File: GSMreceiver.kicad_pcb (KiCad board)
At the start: 2 copper layers, 69 x 83 mm, 136 parts, among them J1 Conn_01x06_Pin, J10 Conn_01x05, J11 Conn_DEGSON_01x02_Pin, J2 Conn_02x02_2.54, J3 Conn_DEGSON_01x02_Pin, J4 Conn_DEGSON_01x02_Pin, J5 Conn_DEGSON_01x02_Pin, J6 Conn_DEGSON_01x02_Pin, J7 Conn_DEGSON_01x02_Pin, J8 1042240820, J9 HJ-SMA405, Q1 BC848, Q2 BC848, SW1 SM5-180UP-1, U1 STM32L052C8Tx, U10 TLV76033, U2 PRAG71S, U3 PRAG71S, U4 PRAG71S, U5 PRAG71S, U6 TPS62177DQC, U7 TPS5430DDA, U8 SIM800C, U9 ST485E, Y1 4 MHz, Y2 32768 kHz

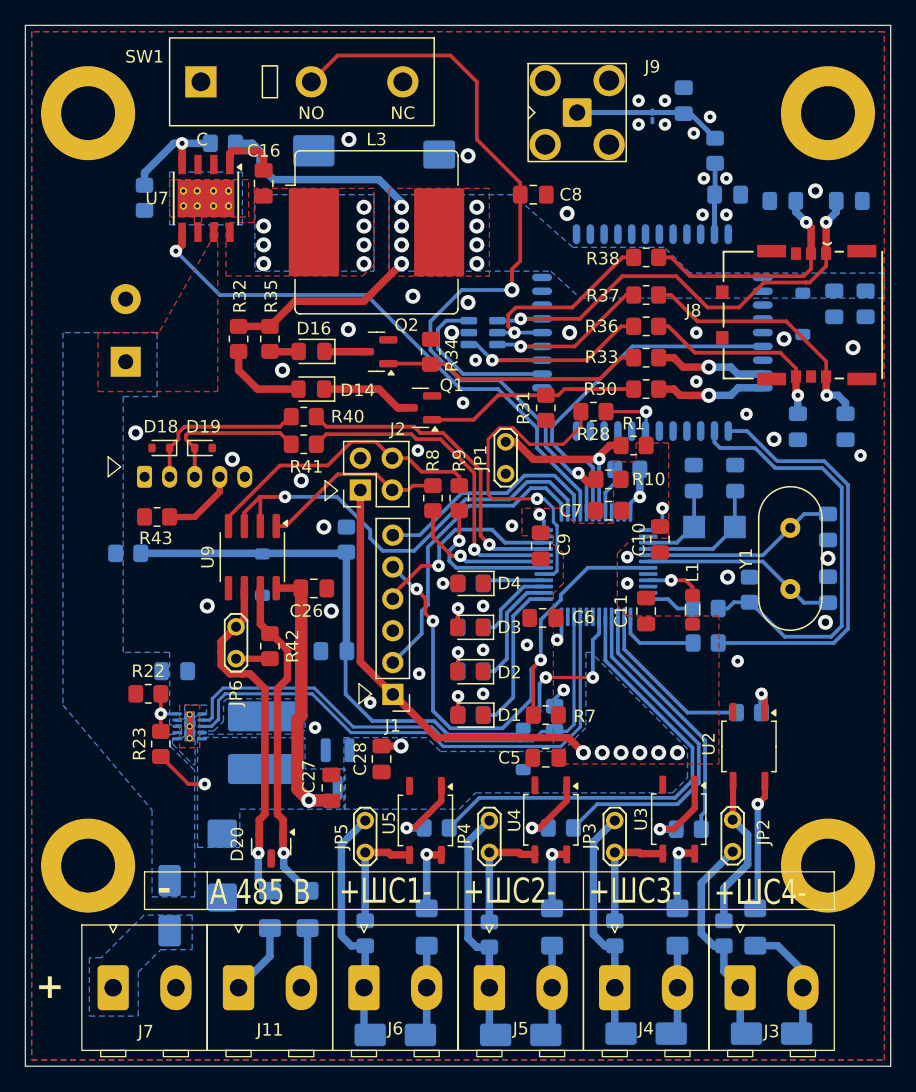
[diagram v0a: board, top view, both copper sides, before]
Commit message: Move to SIM800C-DS and two SIM
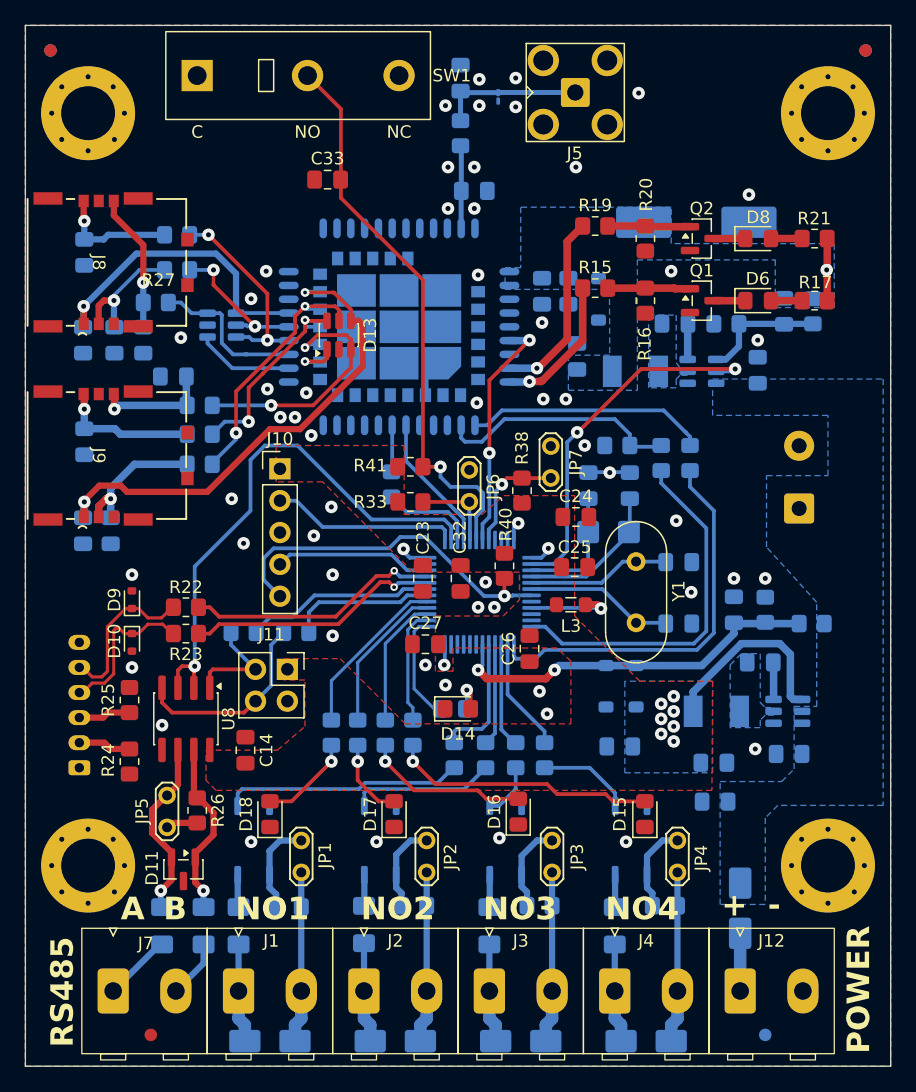
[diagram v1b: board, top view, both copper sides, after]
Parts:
- removed U10: TLV76033, Package_TO_SOT_SMD:SOT-23_Handsoldering
- added C29: 20pF, Capacitor_SMD:C_0805_2012Metric_Pad1.18x1.45mm_HandSolder, B.Cu at (80.1, 70.7)
- added C30: 12.5pF, Capacitor_SMD:C_0805_2012Metric_Pad1.18x1.45mm_HandSolder, B.Cu at (72.9, 59.7)
- added C31: 12.5pF, Capacitor_SMD:C_0805_2012Metric_Pad1.18x1.45mm_HandSolder, B.Cu at (76.2, 59.7)
- added C32: 100nF, Capacitor_SMD:C_0805_2012Metric_Pad1.18x1.45mm_HandSolder, F.Cu at (62.7, 67.1)
- added C33: 100nF, Capacitor_SMD:C_0805_2012Metric_Pad1.18x1.45mm_HandSolder, F.Cu at (52.1, 35.3)
- added C34: 1000uFx35V, Capacitor_THT:CP_Radial_D12.5mm_P5.00mm, B.Cu at (89.7, 61.5)
- added C35: 470nFx50V, Capacitor_SMD:C_0805_2012Metric_Pad1.18x1.45mm_HandSolder, B.Cu at (83.0, 84.9)
- added C36: 100nF, Capacitor_SMD:C_0805_2012Metric_Pad1.18x1.45mm_HandSolder, B.Cu at (84.5, 69.6)
- added D21: SS26, Diode_SMD:D_SMA, B.Cu at (85.0, 93.4)
- added FID1: Fiducial, Fiducial:Fiducial_1mm_Mask2mm, F.Cu at (29.8, 24.8)
- added FID2: Fiducial, Fiducial:Fiducial_1mm_Mask2mm, F.Cu at (95.2, 24.7)
- added FID3: Fiducial, Fiducial:Fiducial_1mm_Mask2mm, F.Cu at (37.5, 103.5)
- added FID4: Fiducial, Fiducial:Fiducial_1mm_Mask2mm, B.Cu at (88.0, 103.0)
- added FID5: Fiducial, Fiducial:Fiducial_1mm_Mask2mm, B.Cu at (30.0, 25.0)
- added FID6: Fiducial, Fiducial:Fiducial_1mm_Mask2mm, B.Cu at (95.0, 25.0)
- added J12: DG390-5.0-02P, footprints:DEGSON_DG390-5.0-02P_1x02_P5.0mm_Vertical, F.Cu at (85.0, 100.0)
- added JP7: Jumper_2_Open, TestPoint:TestPoint_2Pads_Pitch2.54mm_Drill0.8mm, F.Cu at (69.9, 56.5)
- added R44: 1M, Resistor_SMD:R_0805_2012Metric_Pad1.20x1.40mm_HandSolder, B.Cu at (87.0, 69.6)
- added R45: 1M, Resistor_SMD:R_0805_2012Metric_Pad1.20x1.40mm_HandSolder, B.Cu at (90.7, 70.7)
- C1: value 20pF -> 10uF
- C10: value 100nF -> 10pF; moved to B.Cu
- C11: value 100nF -> 33pF; moved to B.Cu
- C12: value 1000uFx35V -> 10pF; footprint Capacitor_THT:CP_Radial_D12.5mm_P5.00mm -> Capacitor_SMD:C_0805_2012Metric_Pad1.18x1.45mm_HandSolder
- C13: value 470nFx50V -> 10pF
- C14, R15: moved to F.Cu
- C15: value CA45-C010K107T -> 100nF; footprint Capacitor_Tantalum_SMD:CP_EIA-6032-28_Kemet-C_Pad2.25x2.35mm_HandSolder -> Capacitor_SMD:C_0805_2012Metric_Pad1.18x1.45mm_HandSolder
- C16: value 10nF -> 22pF; moved to B.Cu
- C17: value 470uFx6.3V -> 22pF; footprint Capacitor_Tantalum_SMD:CP_EIA-7343-30_AVX-N_Pad2.25x2.55mm_HandSolder -> Capacitor_SMD:C_0805_2012Metric_Pad1.18x1.45mm_HandSolder
- C18, C22: value 10pF -> 22pF
- C19: value 33pF -> 100nF
- C2: value 20pF -> 100nF
- C20: value 100nF -> 22pF
- C23, C24: value 22pF -> 100nF; moved to F.Cu
- C25: value 10pF -> 100nF; moved to F.Cu
- C28: value 100nF -> 20pF; moved to B.Cu
- C3, C4: value 12.5pF -> 22uF
- C5: value 100nF -> 10uF; moved to B.Cu
- C6, C8: moved to B.Cu
- C7: value 100nF -> 100pF; moved to B.Cu
- C9: value 100nF -> 1000uF x 10V; footprint Capacitor_SMD:C_0805_2012Metric_Pad1.18x1.45mm_HandSolder -> Capacitor_SMD:CP_Elec_10x10.5; moved to B.Cu
- D1: value GNL-0805UEC -> SMAJ30CA; footprint LED_SMD:LED_0805_2012Metric_Pad1.15x1.40mm_HandSolder -> Diode_SMD:D_SMA; moved to B.Cu
- D10, D9: value SMAJ30CA -> ESD321DYAR; footprint Diode_SMD:D_SMA -> Diode_SMD:D_SOD-523; moved to F.Cu
- D11: value SS26 -> SM712-02HTG; footprint Diode_SMD:D_SMA -> Package_TO_SOT_SMD:SOT-23; moved to F.Cu
- D12: value B340 -> ESDA6V1-5SC6; footprint Diode_SMD:D_SMC -> Package_TO_SOT_SMD:SOT-23-6
- D13: value MMSZ5231BT1G -> ESDA6V1-5SC6; footprint Diode_SMD:D_SOD-123 -> Package_TO_SOT_SMD:SOT-23-6; moved to F.Cu
- D14, D16: value LED_RED -> FYLS-0805PGC
- D15: value ESDA6V1-5SC6 -> FYLS-0805PGC; footprint Package_TO_SOT_SMD:SOT-23-6 -> LED_SMD:LED_0805_2012Metric_Pad1.15x1.40mm_HandSolder; moved to F.Cu
- D17: value LXES1UTAA1-157 -> FYLS-0805PGC; footprint Diode_SMD:D_01005_0402Metric_Pad0.57x0.30mm_HandSolder -> LED_SMD:LED_0805_2012Metric_Pad1.15x1.40mm_HandSolder; moved to F.Cu
- D18: value ESD321DYAR -> FYLS-0805URC; footprint Diode_SMD:D_SOD-523 -> LED_SMD:LED_0805_2012Metric_Pad1.15x1.40mm_HandSolder
- D19: value ESD321DYAR -> MBR0580; footprint Diode_SMD:D_SOD-523 -> Diode_SMD:D_SOD-123; moved to B.Cu
- D2, D3, D4: value GNL-0805PGC-TL -> SMAJ30CA; footprint LED_SMD:LED_0805_2012Metric_Pad1.15x1.40mm_HandSolder -> Diode_SMD:D_SMA; moved to B.Cu
- D20: value SM712_SOT23 -> MBR0580; footprint Package_TO_SOT_SMD:SOT-23 -> Diode_SMD:D_SOD-123; moved to B.Cu
- D5: value MBR0580 -> MMSZ5231BT1G
- D6: value MBR0580 -> FYLS-0805URC; footprint Diode_SMD:D_SOD-123 -> LED_SMD:LED_0805_2012Metric_Pad1.15x1.40mm_HandSolder; moved to F.Cu
- D7: value SMAJ30CA -> LXES1UTAA1-157; footprint Diode_SMD:D_SMA -> Diode_SMD:D_01005_0402Metric_Pad0.57x0.30mm_HandSolder
- D8: value SMAJ30CA -> FYLS-0805URC; footprint Diode_SMD:D_SMA -> LED_SMD:LED_0805_2012Metric_Pad1.15x1.40mm_HandSolder; moved to F.Cu
- J1: value Conn_01x06_Pin -> DG390-5.0-02P; footprint Connector_PinHeader_2.54mm:PinHeader_1x06_P2.54mm_Vertical -> footprints:DEGSON_DG390-5.0-02P_1x02_P5.0mm_Vertical
- J10: value Conn_01x05 -> Conn_01x05_Pin; footprint Connector_JST:JST_PH_B5B-PH-K_1x05_P2.00mm_Vertical -> Connector_PinHeader_2.54mm:PinHeader_1x05_P2.54mm_Vertical; moved to F.Cu
- J11: value Conn_DEGSON_01x02_Pin -> Conn_02x02_2.54; footprint footprints:DEGSON_DG390-5.0-02P_1x02_P5.0mm_Vertical -> Connector_PinSocket_2.54mm:PinSocket_2x02_P2.54mm_Vertical
- J2: value Conn_02x02_2.54 -> DG390-5.0-02P; footprint Connector_PinSocket_2.54mm:PinSocket_2x02_P2.54mm_Vertical -> footprints:DEGSON_DG390-5.0-02P_1x02_P5.0mm_Vertical
- J3, J4, J7: value Conn_DEGSON_01x02_Pin -> DG390-5.0-02P
- J5: value Conn_DEGSON_01x02_Pin -> HJ-SMA405; footprint footprints:DEGSON_DG390-5.0-02P_1x02_P5.0mm_Vertical -> footprints:SMA_HJ-SMA405
- J6: value Conn_DEGSON_01x02_Pin -> Conn_01x06; footprint footprints:DEGSON_DG390-5.0-02P_1x02_P5.0mm_Vertical -> Connector_JST:JST_PH_B6B-PH-K_1x06_P2.00mm_Vertical; moved to B.Cu
- J9: value HJ-SMA405 -> 1042240820; footprint footprints:SMA_HJ-SMA405 -> footprints:1042240820_MOLEX
- L1: value MLZ2012M100WT000 -> CSAB0420-3R3M; footprint Inductor_SMD:L_0805_2012Metric_Pad1.05x1.20mm_HandSolder -> footprints:CSAB0420-4.4x4.4mm; moved to B.Cu
- L2: value KSE-CD5D18NP-220NC -> CSAB0420-100M; footprint Inductor_SMD:L_Cenker_CKCS6028 -> footprints:CSAB0420-4.4x4.4mm
- L3: value 22uH -> MLZ2012M100WT000; footprint Inductor_SMD:L_Bourns_SRR1208_12.7x12.7mm -> Inductor_SMD:L_0805_2012Metric_Pad1.05x1.20mm_HandSolder
- R1: value 100k -> 2k7; moved to B.Cu
- R10: value 100k -> 51k; moved to B.Cu
- R11, R13, R14: value 3k3 -> 1k
- R12: value 3k3 -> 5k6
- R16: value 4k7 -> 47k; moved to F.Cu
- R17: value 4k7 -> 470; moved to F.Cu
- R18: value 4k7 -> 0
- R19: value 100k -> 4k7; moved to F.Cu
- R2, R3, R4: value 680 -> 2k7
- R20: value 1M -> 47k; moved to F.Cu
- R21: value 100k -> 470; moved to F.Cu
- R22: value 130k -> 51
- R23: value 680k -> 51
- R24: value 4k3 -> 5k1; moved to F.Cu
- R25: value 10k -> 5k1; moved to F.Cu
- R26: value 1k -> 680; moved to F.Cu
- R27: value 5k6 -> 51
- R28: value 1k -> 51; moved to B.Cu
- R29: value 1k -> 51
- R30: value 4k7 -> 51; moved to B.Cu
- R31: value 47k -> 51; moved to B.Cu
- R32: value 470 -> 51; moved to B.Cu
- R33: value 4k7 -> 100k
- R34: value 47k -> 680; moved to B.Cu
- R35: value 470 -> 680; moved to B.Cu
- R36, R37: value 51 -> 680; moved to B.Cu
- R38, R40, R41: value 51 -> 100k
- R39: value 0 -> 680
- R42: value 680 -> 51; moved to B.Cu
- R43: value 5k1 -> 51; moved to B.Cu
- R5: value 680 -> 4k7
- R6: value 10k -> 4k7
- R7: value 100k -> 4k7; moved to B.Cu
- R8: value 51 -> 4k7; moved to B.Cu
- R9: value 51 -> 205k; moved to B.Cu
- U1: value STM32L052C8Tx -> PRAB34S; footprint Package_QFP:LQFP-48_7x7mm_P0.5mm -> Package_SO:SOP-4_3.8x4.1mm_P2.54mm
- U2, U3, U4: value PRAG71S -> PRAB34S; moved to B.Cu
- U5: value PRAG71S -> AP63203WU; footprint Package_SO:SOP-4_3.8x4.1mm_P2.54mm -> Package_TO_SOT_SMD:TSOT-23-6; moved to B.Cu
- U6: value TPS62177DQC -> AP63200WU; footprint Package_SON:WSON-10-1EP_2x3mm_P0.5mm_EP0.84x2.4mm_ThermalVias -> Package_TO_SOT_SMD:TSOT-23-6
- U7: value TPS5430DDA -> SIM800C-DS; footprint Package_SO:TI_SO-PowerPAD-8_ThermalVias -> footprints:SIMCom_SIM800C-DS; moved to B.Cu
- U8: value SIM800C -> XR3072XIDTR-F; footprint RF_GSM:SIMCom_SIM800C -> Package_SO:SOIC-8_3.9x4.9mm_P1.27mm; moved to F.Cu
- U9: value ST485E -> STM32L072CBT6; footprint Package_SO:SOIC-8_3.9x4.9mm_P1.27mm -> Package_QFP:LQFP-48_7x7mm_P0.5mm; moved to B.Cu
- moved D7 77.8 mm to (65.7, 28.7), turned to 90 degrees
- moved J5 71.7 mm to (71.8, 28.4)
- moved C19 65.0 mm to (32.6, 63.3)
- moved C20 64.5 mm to (34.8, 63.3), turned to 90 degrees
- moved R18 64.3 mm to (62.7, 31.6), turned to 90 degrees
- moved D8 64.0 mm to (86.4, 40.0), turned to 0 degrees
- moved D17 59.3 mm to (57.4, 85.9)
- moved C21 58.9 mm to (32.7, 56.2), turned to 90 degrees
- moved R17 56.8 mm to (90.9, 45.0), turned to 180 degrees
- moved J8 55.7 mm to (34.5, 41.9), turned to -90 degrees
- moved R39 55.6 mm to (52.4, 79.4), turned to -90 degrees
- moved C18 55.2 mm to (37.4, 48.1)
- moved R27 52.6 mm to (38.4, 45.1), turned to 180 degrees
- moved C13 52.5 mm to (62.7, 27.2), turned to -90 degrees
- moved R15 52.5 mm to (73.4, 44.0), turned to 0 degrees
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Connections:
- C1 pad 2: Net-(U1-PH0) -> /Power_3.3V (page 3)/VBAT_IN
- C10 pad 2: +3V3 -> +4V
- C11 pad 2: +3V3 -> +4V
- C12 pad 1: /IN_OUT/VBAT_OUT -> GNDD
- C12 pad 2: GNDD -> Net-(U7-GSM_ANT)
- C13 pad 1: /IN_OUT/VBAT_OUT -> GNDD
- C13 pad 2: GNDD -> Net-(D7-A2)
- C14 pad 2: /BATTERY_LEVEL -> +3V3
- C15 pad 1: +5V -> GNDD
- C15 pad 2: GNDD -> /RFmodule/SIM1_VDD
- C16 pad 1: Net-(U7-BOOT) -> GNDD
- C16 pad 2: Net-(D12-K) -> /SIMcard1/CARD_RST
- C17 pad 1: +4V -> GNDD
- C17 pad 2: GNDD -> /SIMcard1/CARD_CLK
- C18 pad 2: +4V -> /SIMcard1/CARD_DATA
- C19 pad 2: +4V -> /RFmodule/SIM2_VDD
- C2 pad 1: GNDD -> /Power_3.3V (page 3)/3V3-BST
- C2 pad 2: Net-(U1-PH1) -> /Power_3.3V (page 3)/3V3-SW
- C20 pad 2: Net-(D15-IO3) -> /SIMcard2/CARD_RST
- C21 pad 2: /RFmodule/CARD_RST -> /SIMcard2/CARD_CLK
- C22 pad 2: Net-(U8-GSM_ANT) -> /SIMcard2/CARD_DATA
- C23 pad 2: /RFmodule/CARD_CLK -> +3V3
- C24 pad 2: /RFmodule/CARD_DATA -> +3V3
- C25 pad 2: Net-(D17-A2) -> +3V3
- C26 pad 2: +5V -> +3V3
- C27 pad 2: +5V -> +3V3
- C28 pad 2: +3V3 -> Net-(U9-PH0)
- C3 pad 2: Net-(U1-PC14) -> +3V3
- C4 pad 2: Net-(U1-PC15) -> +3V3
- C5 pad 1: +3V3 -> GNDD
- C5 pad 2: GNDD -> /Power_3.3V (page 3)/VBAT_IN
- C6 pad 1: GNDD -> Net-(U6-BST)
- C6 pad 2: +3V3 -> /Power_4V/4V-SW
- C7 pad 1: GNDD -> /Power_4V/4V-FB
- C7 pad 2: +3V3 -> +4V
- C8 pad 2: /TAMPER -> +4V
- C9 pad 1: GNDD -> +4V
- C9 pad 2: +3V3 -> GNDD
- D1 pad 1: GNDD -> Net-(D1-A1)
- D1 pad 2: Net-(D1-A) -> Net-(D1-A2)
- D10 pad 1: Net-(D10-A1) -> /USB/D-
- D10 pad 2: Net-(D10-A2) -> GNDD
- D11 pad 1: /IN_OUT/VBAT_OUT -> /RS485/RS485_N
- D11 pad 2: Net-(D11-A) -> /RS485/RS485_P
- D12 pad 1: Net-(D12-K) -> /RFmodule/SIM1_DET
- D13 pad 1: +4V -> /RFmodule/SIM2_DET
- D14 pad 1: Net-(D14-K) -> GNDD
- D15 pad 1: Net-(D15-IO1) -> GNDD
- D15 pad 2: GNDD -> Net-(D15-A)
- D16 pad 1: Net-(D16-K) -> GNDD
- D17 pad 2: Net-(D17-A2) -> Net-(D17-A)
- D18 pad 1: /Interface/D+ -> GNDD
- D18 pad 2: GNDD -> Net-(D18-A)
- D19 pad 1: /Interface/D- -> +3V3
- D19 pad 2: GNDD -> /BATTERY_LEVEL
- D2 pad 1: GNDD -> Net-(D2-A1)
- D2 pad 2: Net-(D2-A) -> Net-(D2-A2)
- D20 pad 1: /Interface/RS485_N -> /BATTERY_LEVEL
- D20 pad 2: /Interface/RS485_P -> GNDD
- D3 pad 1: GNDD -> Net-(D3-A1)
- D3 pad 2: Net-(D3-A) -> Net-(D3-A2)
- D4 pad 1: GNDD -> Net-(D4-A1)
- D4 pad 2: Net-(D4-A) -> Net-(D4-A2)
- D5 pad 1: +3V3 -> +4V
- D5 pad 2: /BATTERY_LEVEL -> GNDD
- D6 pad 1: /BATTERY_LEVEL -> Net-(D6-K)
- D6 pad 2: GNDD -> Net-(D6-A)
- D7 pad 1: Net-(D7-A1) -> GNDD
- D8 pad 1: Net-(D8-A1) -> Net-(D8-K)
- D8 pad 2: Net-(D8-A2) -> Net-(D8-A)
- D9 pad 1: Net-(D9-A1) -> /USB/D+
- D9 pad 2: Net-(D9-A2) -> GNDD
- F1 pad 1: Net-(U2-VEE) -> Net-(U1-VEE)
- F1 pad 2: Net-(D7-A1) -> Net-(D1-A1)
- F2 pad 1: Net-(U3-VEE) -> Net-(U2-VEE)
- F2 pad 2: Net-(D8-A1) -> Net-(D2-A1)
- F3 pad 1: Net-(U4-VEE) -> Net-(U3-VEE)
- F3 pad 2: Net-(D9-A1) -> Net-(D3-A1)
- F4 pad 1: Net-(U5-VEE) -> Net-(U4-VEE)
- F4 pad 2: Net-(D10-A1) -> Net-(D4-A1)
- F5 pad 1: /Interface/RS485_P -> /RS485/RS485_P
- F5 pad 2: /Interface/RS485+ -> /RS485/RS485+
- F6 pad 1: /Interface/RS485_N -> /RS485/RS485_N
- F6 pad 2: /Interface/RS485- -> /RS485/RS485-
- J1 pad 1: +3V3 -> Net-(D1-A1)
- J1 pad 2: /SWCLK -> Net-(D1-A2)
- J10 pad 1: GNDD -> +3V3
- J10 pad 2: /Interface/D+ -> /MCU/SWCLK
- J10 pad 3: /Interface/D- -> GNDD
- J10 pad 4: Net-(J10-Pin_4) -> /MCU/SWDIO
- J10 pad 5: unconnected-(J10-Pin_5-Pad5) -> /MCU/NRST
- J11 pad 1: /Interface/RS485+ -> +3V3
- J11 pad 2: /Interface/RS485- -> /UART1_RX
- J2 pad 1: +3V3 -> Net-(D2-A1)
- J2 pad 2: /UART1_RX -> Net-(D2-A2)
- J3 pad 1: Net-(D7-A2) -> Net-(D3-A1)
- J3 pad 2: Net-(D7-A1) -> Net-(D3-A2)
- J4 pad 1: Net-(D8-A2) -> Net-(D4-A1)
- J4 pad 2: Net-(D8-A1) -> Net-(D4-A2)
- J5 pad 1: Net-(D9-A2) -> Net-(D7-A2)
- J5 pad 2: Net-(D9-A1) -> GNDD
- J6 pad 1: Net-(D10-A2) -> unconnected-(J6-Pin_1-Pad1)
- J6 pad 2: Net-(D10-A1) -> Net-(J6-Pin_2)
- J7 pad 1: Net-(D11-A) -> /RS485/RS485+
- J7 pad 2: GNDD -> /RS485/RS485-
- J8 pad S1: Net-(D15-IO3) -> /RFmodule/SIM1_VDD
- J8 pad S2: /RFmodule/CARD_RST -> /SIMcard1/CARD_RST
- J8 pad S3: /RFmodule/CARD_CLK -> /SIMcard1/CARD_CLK
- J8 pad S6: /RFmodule/CARD_DATA -> /SIMcard1/CARD_DATA
- JP1 pad 1: GNDD -> Net-(JP1-A)
- JP1 pad 2: Net-(JP1-B) -> Net-(D1-A2)
- JP2 pad 2: Net-(D7-A2) -> Net-(D2-A2)
- JP3 pad 2: Net-(D8-A2) -> Net-(D3-A2)
- JP4 pad 2: Net-(D9-A2) -> Net-(D4-A2)
- JP5 pad 2: Net-(D10-A2) -> /RS485/RS485_P
- JP6 pad 1: Net-(JP6-A) -> GNDD
- JP6 pad 2: /Interface/RS485_P -> Net-(JP6-B)
- L1 pad 1: +3V3 -> /Power_3.3V (page 3)/3V3-SW
- L1 pad 2: Net-(U1-VDDA) -> +3V3
- L2 pad 1: Net-(U6-SW) -> /Power_4V/4V-SW
- L2 pad 2: +5V -> +4V
- L3 pad 1: Net-(D12-K) -> +3V3
- L3 pad 2: +4V -> Net-(U9-VDDA)
- Q1 pad 3: Net-(D14-K) -> Net-(D6-K)
- Q2 pad 3: Net-(D16-K) -> Net-(D8-K)
- R1 pad 1: +3V3 -> /DOUT1
- R1 pad 2: Net-(JP1-B) -> Net-(U1-A)
- R10 pad 1: +3V3 -> GNDD
- R10 pad 2: /TAMPER -> /Power_4V/4V-FB
- R11 pad 1: /DOUT1 -> /UART2_TX
- R11 pad 2: Net-(U2-A) -> Net-(U7-UART1_RXD)
- R12 pad 1: /DOUT2 -> GNDD
- R12 pad 2: Net-(U3-A) -> Net-(U7-UART1_RXD)
- R13 pad 1: /DOUT3 -> /UART2_RI
- R13 pad 2: Net-(U4-A) -> Net-(U7-UART1_RI)
- R14 pad 1: /DOUT4 -> /UART2_RX
- R14 pad 2: Net-(U5-A) -> Net-(U7-UART1_TXD)
- R15 pad 1: Net-(JP2-A) -> /RFmodule/STATUS
- R15 pad 2: Net-(D7-A2) -> Net-(Q1-B)
- R16 pad 1: Net-(JP3-A) -> Net-(Q1-B)
- R16 pad 2: Net-(D8-A2) -> GNDD
- R17 pad 1: Net-(JP4-A) -> +4V
- R17 pad 2: Net-(D9-A2) -> Net-(D6-A)
- R18 pad 1: Net-(JP5-A) -> Net-(U7-GSM_ANT)
- R18 pad 2: Net-(D10-A2) -> Net-(D7-A2)
- R19 pad 1: /BATTERY_LEVEL -> /RFmodule/NETLIGHT
- R19 pad 2: GNDD -> Net-(Q2-B)
- R2 pad 1: Net-(U1-PB12) -> /DOUT2
- R2 pad 2: Net-(D1-A) -> Net-(U2-A)
- R20 pad 1: /BATTERY_LEVEL -> Net-(Q2-B)
- R20 pad 2: /IN_OUT/VBAT_OUT -> GNDD
- R21 pad 1: /PWR_GOOD -> +4V
- R21 pad 2: +3V3 -> Net-(D8-A)
- R22 pad 1: GNDD -> /USB_D+
- R22 pad 2: Net-(U6-FB) -> /USB/D+
- R23 pad 1: Net-(U6-FB) -> /USB_D-
- R23 pad 2: +5V -> /USB/D-
- R24 pad 1: GNDD -> Net-(J6-Pin_2)
- R24 pad 2: Net-(U7-VSENSE) -> GNDD
- R25 pad 1: Net-(U7-VSENSE) -> Net-(J6-Pin_3)
- R25 pad 2: +4V -> GNDD
- R26 pad 1: /UART2_TX -> /RS485/RS485_N
- R26 pad 2: Net-(U8-UART1_RXD) -> Net-(JP5-A)
- R27 pad 1: GNDD -> /RFmodule/SIM1_DATA
- R27 pad 2: Net-(U8-UART1_RXD) -> /SIMcard1/CARD_DATA
- R28 pad 1: /UART2_RI -> /RFmodule/SIM1_CLK
- R28 pad 2: Net-(U8-UART1_RI) -> /SIMcard1/CARD_CLK
- R29 pad 1: /UART2_RX -> /RFmodule/SIM1_RST
- R29 pad 2: Net-(U8-UART1_TXD) -> /SIMcard1/CARD_RST
- R3 pad 1: Net-(U1-PB13) -> /DOUT3
- R3 pad 2: Net-(D2-A) -> Net-(U3-A)
- R30 pad 1: /RFmodule/STATUS -> /RFmodule/SIM2_DATA
- R30 pad 2: Net-(Q1-B) -> /SIMcard2/CARD_DATA
- R31 pad 1: Net-(Q1-B) -> /RFmodule/SIM2_CLK
- R31 pad 2: GNDD -> /SIMcard2/CARD_CLK
- R32 pad 1: +4V -> /RFmodule/SIM2_RST
- R32 pad 2: Net-(D14-A) -> /SIMcard2/CARD_RST
- R33 pad 1: /RFmodule/NETLIGHT -> +3V3
- R33 pad 2: Net-(Q2-B) -> Net-(JP6-B)
- R34 pad 1: Net-(Q2-B) -> /MCU/LED1
- R34 pad 2: GNDD -> Net-(D14-A)
- R35 pad 1: +4V -> /MCU/LED2
- R35 pad 2: Net-(D16-A) -> Net-(D15-A)
- R36 pad 1: Net-(D15-IO1) -> /MCU/LED3
- R36 pad 2: /RFmodule/CARD_DATA -> Net-(D16-A)
- R37 pad 1: Net-(D15-IO5) -> /MCU/LED4
- R37 pad 2: /RFmodule/CARD_CLK -> Net-(D17-A)
- R38 pad 1: Net-(D15-IO4) -> +3V3
- R38 pad 2: /RFmodule/CARD_RST -> /MCU/BOOT0
- R39 pad 1: Net-(U8-GSM_ANT) -> /MCU/LED5
- R39 pad 2: Net-(D17-A2) -> Net-(D18-A)
- R4 pad 1: Net-(U1-PB14) -> /DOUT4
- R4 pad 2: Net-(D3-A) -> Net-(U4-A)
- R40 pad 1: /USB_D+ -> +3V3
- R40 pad 2: /Interface/D+ -> /MCU/NRST
- R41 pad 1: /USB_D- -> +3V3
- R41 pad 2: /Interface/D- -> /MCU/TAMPER
- R42 pad 1: /Interface/RS485_N -> Net-(U9-PA10)
- R42 pad 2: Net-(JP6-A) -> /UART1_RX
- R43 pad 1: Net-(J10-Pin_4) -> Net-(U9-PA9)
- R43 pad 2: GNDD -> /UART1_TX
- R5 pad 1: Net-(U1-PB15) -> Net-(JP1-A)
- R5 pad 2: Net-(D4-A) -> Net-(D1-A2)
- R6 pad 1: +3V3 -> Net-(JP2-A)
- R6 pad 2: Net-(U1-BOOT0) -> Net-(D2-A2)
- R7 pad 1: +3V3 -> Net-(JP3-A)
- R7 pad 2: /NRST -> Net-(D3-A2)
- R8 pad 1: Net-(U1-PA10) -> Net-(JP4-A)
- R8 pad 2: /UART1_RX -> Net-(D4-A2)
- R9 pad 1: Net-(U1-PA9) -> /Power_4V/4V-FB
- R9 pad 2: /UART1_TX -> +4V
- SW1 pad 2: /TAMPER -> /MCU/TAMPER
- U1 pad 1: +3V3 -> Net-(U1-A)
- U1 pad 2: unconnected-(U1-PC13-Pad2) -> GNDD
- U1 pad 3: Net-(U1-PC14) -> Net-(JP1-A)
- U1 pad 4: Net-(U1-PC15) -> Net-(U1-VEE)
- U5 pad 1: Net-(U5-A) -> +3V3
- U5 pad 2: GNDD -> /Power_3.3V (page 3)/VBAT_IN
- U5 pad 3: Net-(JP5-A) -> /Power_3.3V (page 3)/VBAT_IN
- U5 pad 4: Net-(U5-VEE) -> GNDD
- U6 pad 1: GNDD -> /Power_4V/4V-FB
- U6 pad 2: /IN_OUT/VBAT_OUT -> /4V_ENABLE
- U6 pad 3: /IN_OUT/VBAT_OUT -> /Power_3.3V (page 3)/VBAT_IN
- U6 pad 5: Net-(U6-FB) -> /Power_4V/4V-SW
- U6 pad 6: GNDD -> Net-(U6-BST)
- U7 pad 1: Net-(U7-BOOT) -> Net-(U7-UART1_TXD)
- U7 pad 2: unconnected-(U7-NC-Pad2) -> Net-(U7-UART1_RXD)
- U7 pad 4: Net-(U7-VSENSE) -> unconnected-(U7-UART1_CTS-Pad4)
- U7 pad 5: /4V_ENABLE -> unconnected-(U7-UART1_DCD-Pad5)
- U7 pad 6: GNDD -> /UART2_DTR
- U7 pad 7: /IN_OUT/VBAT_OUT -> Net-(U7-UART1_RI)
- U7 pad 8: Net-(D12-K) -> GNDD
- U7 pad 9: GNDD -> unconnected-(U7-MICP-Pad9)
- U8 pad 1: Net-(U8-UART1_TXD) -> /UART1_RX
- U8 pad 2: Net-(U8-UART1_RXD) -> /RS485_EN
- U8 pad 3: unconnected-(U8-UART1_RTS-Pad3) -> /RS485_EN
- U8 pad 4: unconnected-(U8-UART1_CTS-Pad4) -> /UART1_TX
- U8 pad 5: unconnected-(U8-UART1_DCD-Pad5) -> GNDD
- U8 pad 6: unconnected-(U8-UART1_DTR-Pad6) -> /RS485/RS485_P
- U8 pad 7: Net-(U8-UART1_RI) -> /RS485/RS485_N
- U8 pad 8: GNDD -> +3V3
- U9 pad 1: /UART1_RX -> +3V3
- U9 pad 2: /V_ISO -> /4V_ENABLE
- U9 pad 3: /V_ISO -> Net-(U9-PC14)
- U9 pad 4: /UART1_TX -> Net-(U9-PC15)
- U9 pad 5: GNDD -> Net-(U9-PH0)
- U9 pad 6: /Interface/RS485_P -> Net-(U9-PH1)
- U9 pad 7: /Interface/RS485_N -> /MCU/NRST
- U9 pad 8: +5V -> GNDD
- Y1 pad 1: Net-(U1-PH1) -> Net-(U9-PH1)
- Y1 pad 2: Net-(U1-PH0) -> Net-(U9-PH0)
- Y2 pad 1: Net-(U1-PC15) -> Net-(U9-PC15)
- Y2 pad 2: Net-(U1-PC14) -> Net-(U9-PC14)
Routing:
- net /TAMPER: track 65.0 -> 0.00 mm, vias 2 -> 0
- net /MCU/TAMPER: track 0.00 -> 45.1 mm, vias 0 -> 1
- net /NRST: track 43.9 -> 0.00 mm, vias 3 -> 0
- net /SLEEP: track 43.3 -> 0.00 mm
- net /RS485_EN: track 0.00 -> 43.1 mm, vias 0 -> 1
- net /PWR_GOOD: track 42.5 -> 0.00 mm
- net /RFmodule/SIM2_VDD: track 0.00 -> 40.5 mm, vias 0 -> 2
- net Net-(D15-IO3): track 37.1 -> 0.00 mm, vias 2 -> 0
- net /V_ISO: track 36.8 -> 0.00 mm, vias 1 -> 0
- net Net-(U8-UART1_RXD): track 35.1 -> 0.00 mm
- net Net-(U8-UART1_TXD): track 33.6 -> 0.00 mm
- net /MCU/NRST: track 0.00 -> 28.9 mm, vias 0 -> 1
- net /Interface/RS485_P: track 27.9 -> 0.00 mm, vias 1 -> 0
- net /DOUT4: track 36.9 -> 9.06 mm
- net /BATTERY_LEVEL: track 57.2 -> 30.8 mm
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- added copper zone on B.Cu, net /Power_3.3V (page 3)/3V3-SW
- added copper zone on B.Cu, net /Power_3.3V (page 3)/VBAT_IN
- added copper zone on B.Cu, net /Power_4V/4V-SW
- removed copper zone on F.Cu, net +4V
- removed copper zone on B.Cu, net +5V
- removed copper zone on B.Cu, net /IN_OUT/VBAT_OUT
- removed copper zone on F.Cu, net /IN_OUT/VBAT_OUT
- removed copper zone on B.Cu, net Net-(D11-A)
- removed copper zone on B.Cu, net Net-(D12-K)
- removed copper zone on F.Cu, net Net-(D12-K)
- removed copper zone on B.Cu, net Net-(U6-SW)
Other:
- board text added: "A"
- board text added: "B"
- board text added: "NO1"
- board text added: "NO2"
- board text added: "NO3"
- board text added: "NO4"
- board text added: "POWER"
- board text added: "RS485"
- board text removed: "+ШС1-"
- board text removed: "+ШС2-"
- board text removed: "+ШС3-"
- board text removed: "+ШС4-"
- board text removed: "A 485 B"

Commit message: Kicad 10 update
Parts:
- D11: moved to B.Cu
- moved R43 3.80 mm to (53.4, 71.4)
- moved R42 3.60 mm to (49.0, 71.4)
- moved JP5 0.30 mm to (39.0, 87.0)
- moved D11 0.20 mm to (40.6, 90.1), turned to 90 degrees
- moved JP7 0.20 mm to (70.1, 56.5)
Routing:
- net Net-(U9-PA9): track 11.6 -> 7.50 mm
- net /UART1_TX: track 15.8 -> 19.7 mm
- net Net-(U9-PA10): track 15.1 -> 12.1 mm
- net /UART1_RX: track 8.44 -> 9.14 mm
- net /RS485/RS485_N: track 14.1 -> 14.7 mm
- net /RS485/RS485_P: track 14.5 -> 15.1 mm, vias 1 -> 0

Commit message: Fiducial position move to the observable area
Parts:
- moved FID3 13.9 mm to (42.5, 90.5)
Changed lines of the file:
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@@
 	(footprint "Fiducial:Fiducial_1mm_Mask2mm"
 		(layer "F.Cu")
-		(at 37.5 103.5)
+		(at 42.5 90.5)
 		(descr "Fiducial, circular marking, 1mm bare copper, 2mm soldermask opening (Level A)")
 		(tags "fiducial")

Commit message: Release candidate
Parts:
- C12, C13: footprint Capacitor_SMD:C_0805_2012Metric_Pad1.18x1.45mm_HandSolder -> Capacitor_SMD:C_0603_1608Metric_Pad1.08x0.95mm_HandSolder
- D10, D9, R26, R38: moved to B.Cu
- JP1, JP2, JP3, JP4, JP5, JP6, JP7: footprint TestPoint:TestPoint_2Pads_Pitch2.54mm_Drill0.8mm -> Connector_PinHeader_2.54mm:PinHeader_1x02_P2.54mm_Vertical
- R18: footprint Resistor_SMD:R_0805_2012Metric_Pad1.20x1.40mm_HandSolder -> Resistor_SMD:R_0603_1608Metric_Pad0.98x0.95mm_HandSolder
- R22, R23: footprint Resistor_SMD:R_0805_2012Metric_Pad1.20x1.40mm_HandSolder -> Resistor_SMD:R_0603_1608Metric_Pad0.98x0.95mm_HandSolder; moved to B.Cu
- R5, R6, R7, R8: footprint Resistor_SMD:R_0805_2012Metric_Pad1.20x1.40mm_HandSolder -> Resistor_SMD:R_1206_3216Metric_Pad1.30x1.75mm_HandSolder
- moved C14 4.29 mm to (44.0, 84.8), turned to 90 degrees
- moved J11 4.17 mm to (46.2, 77.5), turned to 180 degrees
- moved R22 3.62 mm to (44.4, 69.9)
- moved R23 3.59 mm to (44.4, 71.5)
- moved C13 3.40 mm to (61.9, 30.5), turned to 0 degrees
- moved R42 3.36 mm to (52.1, 72.7), turned to -90 degrees
- moved D9 2.72 mm to (39.2, 69.1)
- moved D10 2.71 mm to (39.2, 72.4)
- moved R18 1.80 mm to (62.8, 33.4)
- moved R43 1.64 mm to (54.4, 72.7), turned to -90 degrees
- moved JP2 0.80 mm to (60.8, 88.0), turned to 0 degrees
- moved JP3 0.80 mm to (70.8, 88.0), turned to 0 degrees
- moved JP1 0.70 mm to (50.7, 88.0), turned to 0 degrees
- moved JP4 0.70 mm to (80.7, 88.0), turned to 0 degrees
- moved R24 0.40 mm to (35.9, 81.7)
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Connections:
- J11 pad 2: /UART1_RX -> /UART1_TX
- J11 pad 4: /UART1_TX -> /UART1_RX
- JP5 pad 1: Net-(JP5-A) -> /RS485/RS485_P
- JP5 pad 2: /RS485/RS485_P -> Net-(JP5-B)
- R26 pad 2: Net-(JP5-A) -> Net-(JP5-B)
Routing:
- net /UART1_RX: track 9.14 -> 14.0 mm
- net /USB_D+: track 20.3 -> 16.4 mm, vias 1 -> 0
- net /USB_D-: track 20.2 -> 16.4 mm, vias 1 -> 0
- net /USB/D-: track 12.4 -> 15.7 mm
- net Net-(JP5-B): track 0.00 -> 3.27 mm
- net /USB/D+: track 12.8 -> 15.7 mm
- net Net-(JP5-A): track 2.54 -> 0.00 mm
- net Net-(U9-PA10): track 12.1 -> 10.1 mm
- net /MCU/BOOT0: track 9.26 -> 11.1 mm
- net +3V3: track 22.9 -> 24.6 mm
- net Net-(U7-GSM_ANT): track 6.62 -> 4.91 mm
- net /RS485_EN: track 43.1 -> 41.6 mm
- net /RS485/RS485_P: track 15.1 -> 13.9 mm
- net Net-(D7-A2): track 11.6 -> 12.5 mm
- net Net-(JP1-A): track 7.51 -> 6.79 mm
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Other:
- board text added: "SIM1"
- board text added: "SIM2"

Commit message: Proproduction version
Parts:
- removed the C25 at (71.8, 66.2)
- removed the C26 at (68.2, 72.7)
- removed the C27 at (59.9, 72.3)
- removed the D10 at (39.2, 72.4)
- removed the D9 at (39.2, 69.1)
- added C14: 100nF, Capacitor_SMD:C_0805_2012Metric_Pad1.18x1.45mm_HandSolder, B.Cu at (44.9, 81.3)
- added C15: 100nF, Capacitor_SMD:C_0805_2012Metric_Pad1.18x1.45mm_HandSolder, B.Cu at (38.1, 80.2)
- added D20: SMAJ30CA, Diode_SMD:D_SMA, B.Cu at (87.5, 104.0)
- added U8: USBLC6-2SC6, Package_TO_SOT_SMD:SOT-23-6, B.Cu at (37.1, 73.2)
- C25: renamed from C23; moved to B.Cu
- C26: renamed from C24; moved to B.Cu
- C31: renamed from C32; moved to B.Cu
- C32: renamed from C33; moved to B.Cu
- D6: value FYLS-0805URC -> STATUS
- D8: value FYLS-0805URC -> NETLIGHT
- J1: value DG390-5.0-02P -> Relay_1
- J10: value Conn_01x05_Pin -> SWD
- J11: value Conn_02x02_2.54 -> UART1
- J2: value DG390-5.0-02P -> Relay_2
- J3: value DG390-5.0-02P -> Relay_3
- J4: value DG390-5.0-02P -> Relay_4
- J5: value HJ-SMA405 -> RF Antenna
- J6: value Conn_01x06 -> USB-C
- J7: value DG390-5.0-02P -> RS485
- R1, R2, R3, R4: value 2k7 -> 2.7k
- R12: value 5k6 -> 5.6k
- R15, R19, R5, R6, R7, R8: value 4k7 -> 4.7k
- R22: value 51 -> 47k; footprint Resistor_SMD:R_0603_1608Metric_Pad0.98x0.95mm_HandSolder -> Resistor_SMD:R_0805_2012Metric_Pad1.20x1.40mm_HandSolder
- R23: value 51 -> 100k; footprint Resistor_SMD:R_0603_1608Metric_Pad0.98x0.95mm_HandSolder -> Resistor_SMD:R_0805_2012Metric_Pad1.20x1.40mm_HandSolder
- R24, R25: value 5k1 -> 5.1k
- R26: value 680 -> 120
- R44: value 1M -> 100k
- moved JP6 23.6 mm to (58.1, 35.4), turned to -90 degrees
- moved R40 11.4 mm to (54.9, 67.3)
- moved C25 11.3 mm to (51.4, 59.4)
- moved R23 8.83 mm to (38.1, 77.7)
- moved C31 7.59 mm to (55.5, 64.7), turned to 180 degrees
- moved R22 7.35 mm to (41.6, 76.7), turned to 90 degrees
- moved FID4 6.50 mm to (94.5, 102.9)
- moved C32 3.31 mm to (50.5, 32.4)
- moved C26 2.24 mm to (69.7, 62.6), turned to -90 degrees
- moved J6 2.00 mm to (32.3, 80.2)
- moved R24 2.00 mm to (35.9, 79.7)
- moved R25 1.60 mm to (35.9, 75.2)
- moved JP2 1.03 mm to (60.8, 87.0)
- moved JP1 1.00 mm to (50.7, 87.0)
- moved JP3 1.00 mm to (70.8, 87.0)
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- renumbered C14 to C16, C15 to C17, C16 to C18, C17 to C19, C18 to C20, C19 to C21, C20 to C22, C21 to C23, C22 to C24, C28 to C27, C29 to C28, C30 to C29, C31 to C30, C34 to C33, C35 to C34, C36 to C35, D12 to D10, D13 to D11, D14 to D12, D15 to D13, D16 to D14, D17 to D15, D18 to D16, D19 to D17, D20 to D18, D21 to D19, D11 to D9, U9 to U10, U8 to U9
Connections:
- net Net-(D1-A1) renamed /IN_OUT/RELAY1B
- net Net-(D1-A2) renamed /IN_OUT/RELAY1A
- net Net-(D2-A1) renamed /IN_OUT/RELAY2B
- net Net-(D2-A2) renamed /IN_OUT/RELAY2A
- net Net-(D21-A) renamed /Power_input/Vsupply
- net Net-(D3-A1) renamed /IN_OUT/RELAY3B
- net Net-(D3-A2) renamed /IN_OUT/RELAY3A
- net Net-(D4-A1) renamed /IN_OUT/RELAY4B
- net Net-(D4-A2) renamed /IN_OUT/RELAY4A
- net Net-(J6-Pin_2) renamed /USB/USB_CC1
- net Net-(J6-Pin_3) renamed /USB/USB_CC2
- J6 pad 1: unconnected-(J6-Pin_1-Pad1) -> /USB/USB_VBUS
- J6 pad 4: /USB/D- -> /USB/USB_N
- J6 pad 5: /USB/D+ -> /USB/USB_P
- R22 pad 1: /USB_D+ -> /MCU/VBUS_SENSING
- R22 pad 2: /USB/D+ -> GNDD
- R23 pad 1: /USB_D- -> /MCU/VBUS_SENSING
- R23 pad 2: /USB/D- -> /USB/USB_VBUS
- U10 pad 19: unconnected-(U9-PB1-Pad19) -> /MCU/VBUS_SENSING
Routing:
- net /MCU/VBUS_SENSING: track 0.00 -> 37.1 mm
- net Net-(JP6-B): track 7.24 -> 36.0 mm, vias 0 -> 1
- net /USB/D-: track 15.7 -> 0.00 mm
- net /USB/D+: track 15.7 -> 0.00 mm
- net /USB/USB_VBUS: track 0.00 -> 13.2 mm
- net /MCU/NRST: track 28.9 -> 20.2 mm
- net /USB_D+: track 16.4 -> 24.8 mm
- net /USB_D-: track 16.4 -> 24.6 mm
- net +3V3: track 24.6 -> 30.4 mm
- net /Power_input/Vsupply: track 4.64 -> 8.85 mm
- net /USB/USB_P: track 0.00 -> 3.68 mm
- net /USB/USB_N: track 0.00 -> 3.68 mm
- net Net-(JP1-A): track 6.79 -> 8.37 mm
- net /MCU/TAMPER: track 45.0 -> 46.3 mm, vias 1 -> 2
- net GNDD: track 5.31 -> 6.57 mm, vias 80 -> 84
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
